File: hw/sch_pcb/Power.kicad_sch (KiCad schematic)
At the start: 55 parts, among them J3 HEADER_1x02, U10 TPS563249, U11 LTC3601, U12 NCP1117ST33, U9 LTC3601

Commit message: Renaming project to match name of new revision.
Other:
- title: QFHMIX01D -> QFHMIX01E
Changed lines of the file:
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@@
   (paper "A4")
   (title_block
-    (title "QFHMIX01D")
-    (date "2021-04-21")
+    (title "QFHMIX01E")
+    (date "2022-07-31")
     (comment 2 "Frontend for QFH active antenna")
   )

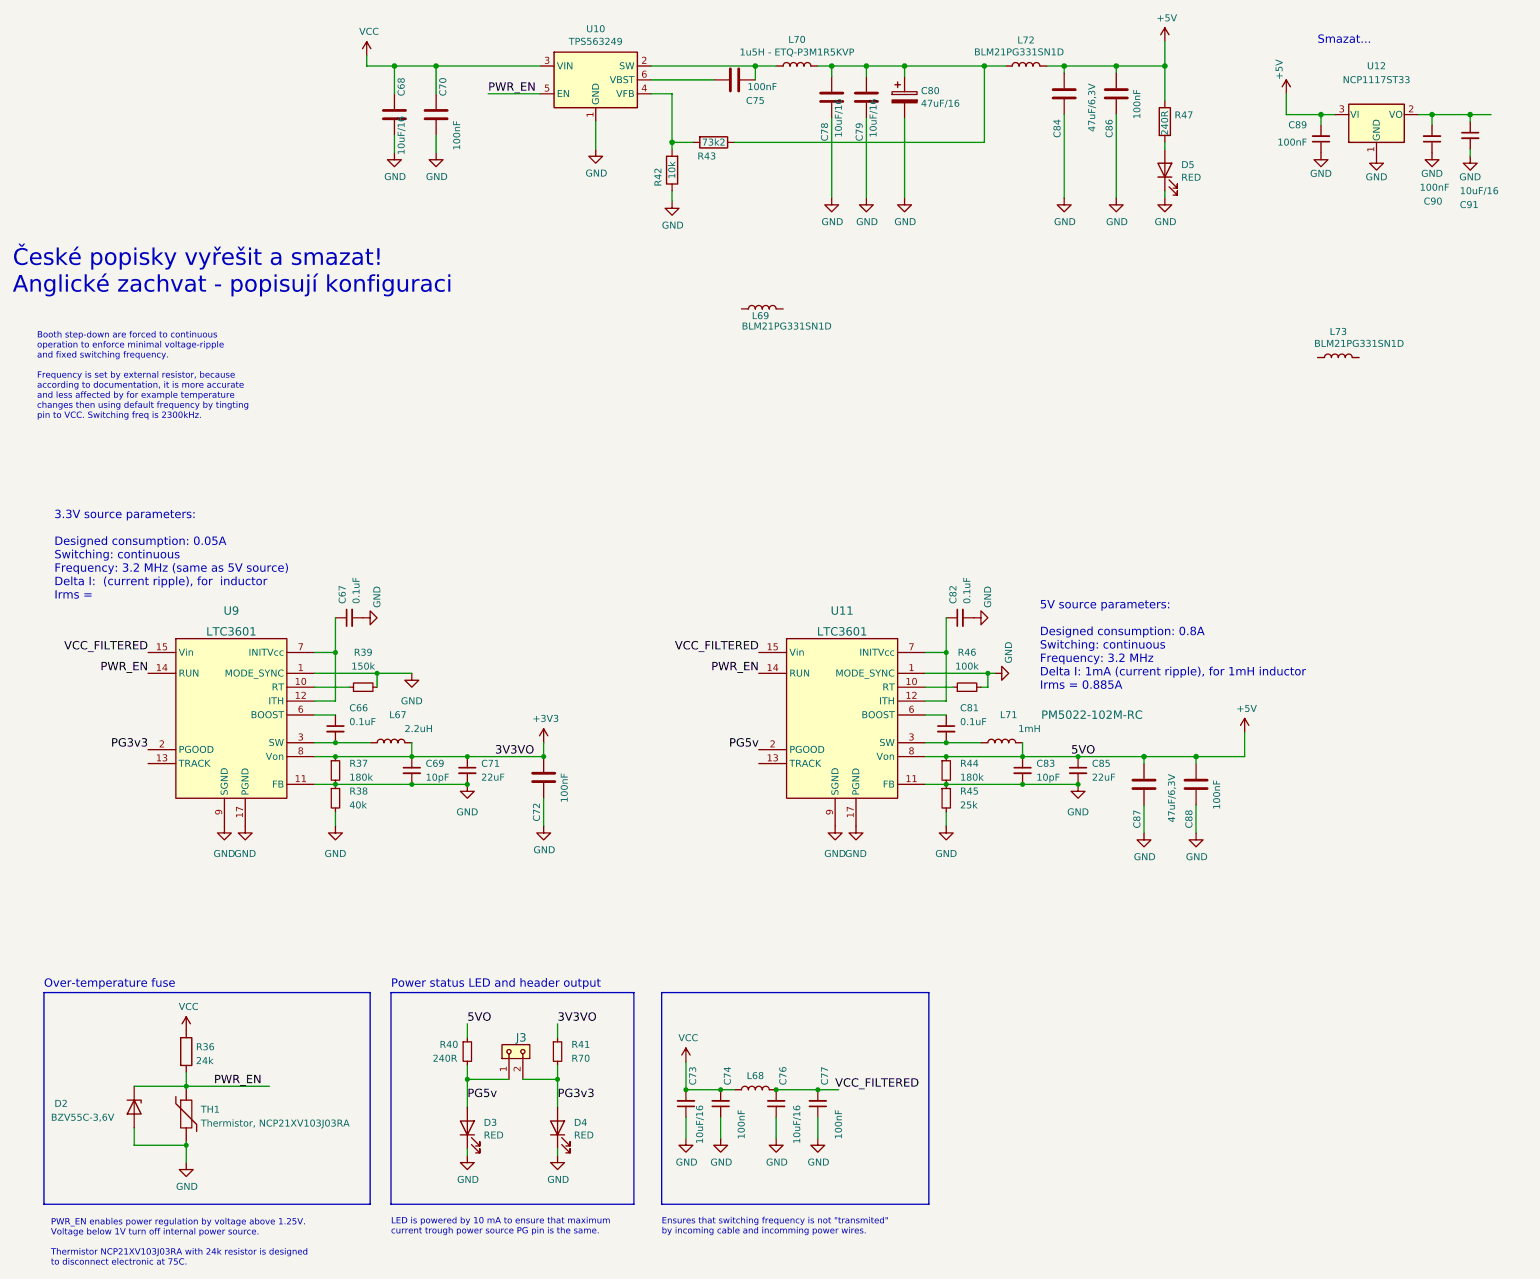
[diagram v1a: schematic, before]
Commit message: Add filter capacitors at swithinch power supply inputs.
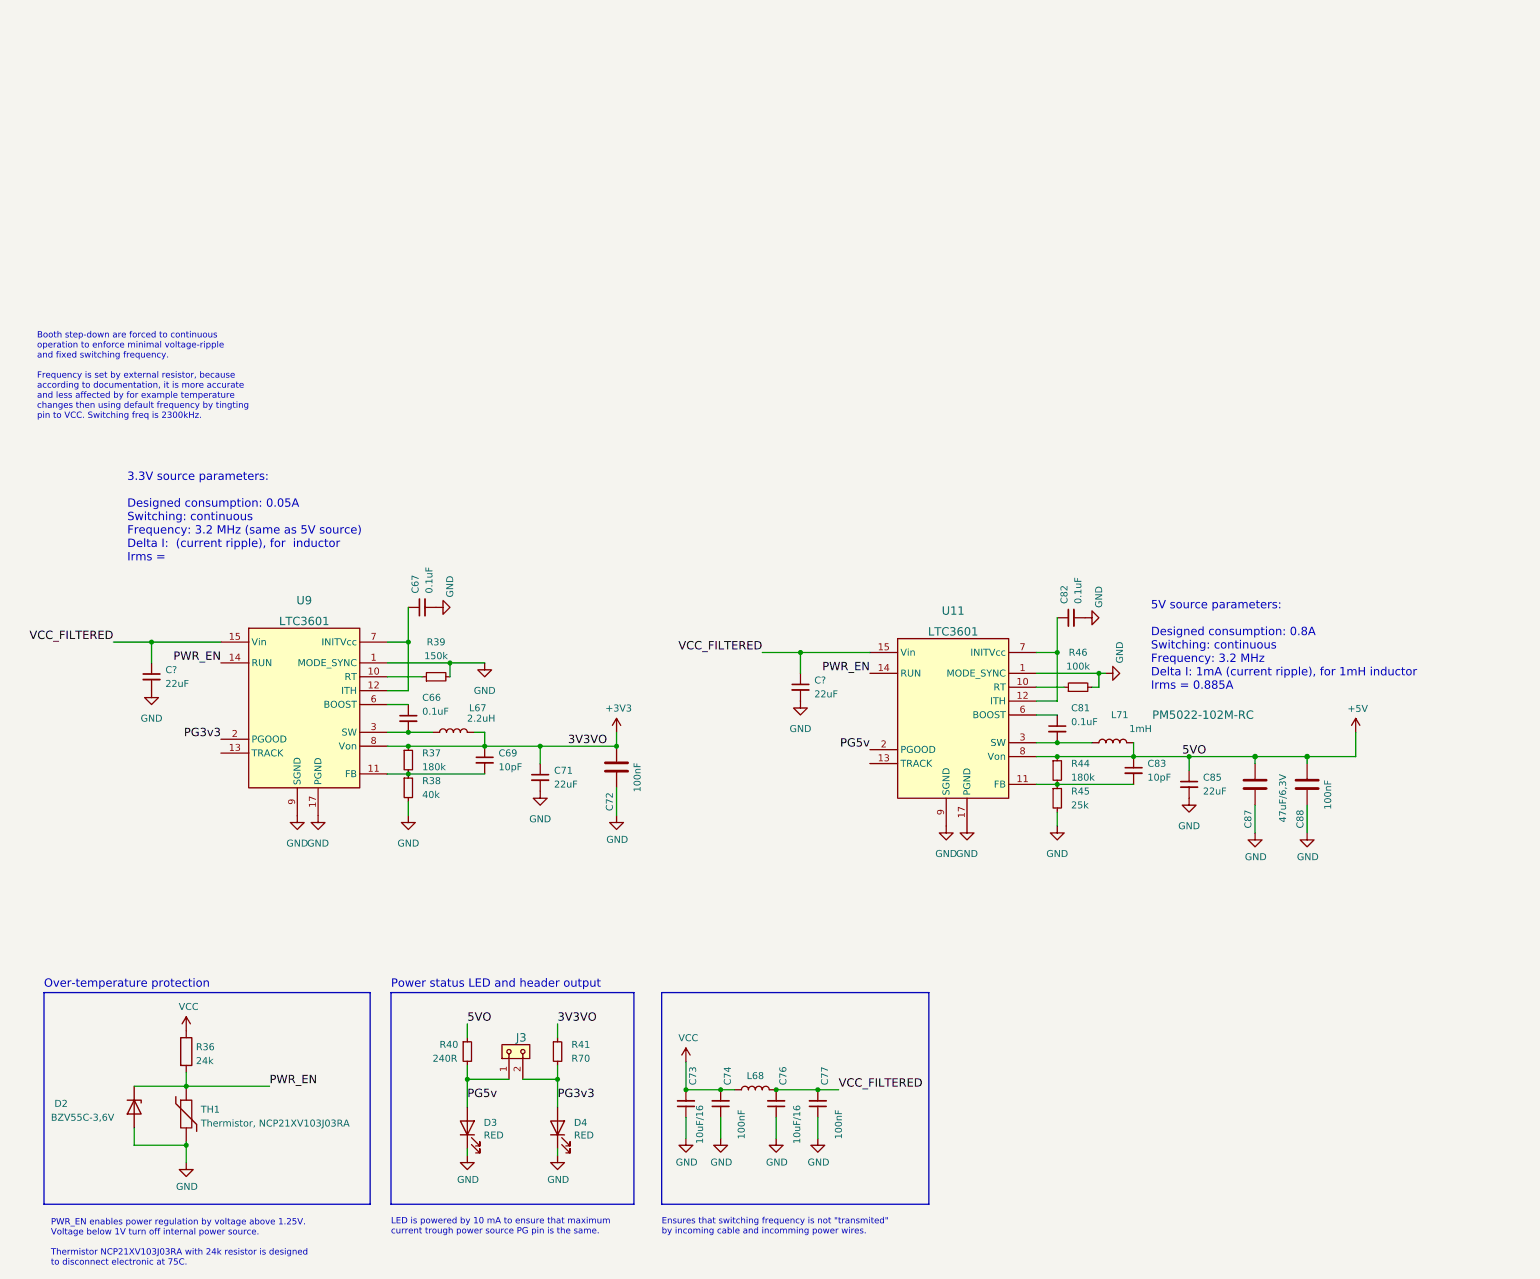
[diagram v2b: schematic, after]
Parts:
- removed C68, C78, C79: 10uF/16, Capacitor_SMD:C_0805_2012Metric, symbol Device:C
- removed C70, C75, C86: 100nF, Capacitor_SMD:C_0603_1608Metric, symbol Device:C
- removed C80: 47uF/16, Mlab_C:TantalC_SizeC_Reflow, symbol Device:CP
- removed C84: 47uF/6,3V, Capacitor_SMD:C_0805_2012Metric, symbol Device:C
- removed C89, C90: 100nF, Capacitor_SMD:C_0603_1608Metric, symbol QFHMIX01C-rescue:C_Small-device-QFHMIX01B-rescue
- removed C91: 10uF/16, Capacitor_SMD:C_0805_2012Metric, symbol QFHMIX01C-rescue:C_Small-device-QFHMIX01B-rescue
- removed D5: RED, Mlab_D:LED_1206, symbol Device:LED
- removed L69: BLM21PG331SN1D, Inductor_SMD:L_0805_2012Metric_Pad1.15x1.40mm_HandSolder, symbol QFHMIX01C-rescue:L-device-QFHMIX01B-rescue
- removed L70: 1u5H - ETQ-P3M1R5KVP, Mlab_L:PCC-M0530M-LP, symbol Device:L
- removed L72, L73: BLM21PG331SN1D, Inductor_SMD:L_0805_2012Metric_Pad1.15x1.40mm_HandSolder, symbol Device:L
- removed R42: 10k, Resistor_SMD:R_0603_1608Metric, symbol Device:R
- removed R43: 73k2, Resistor_SMD:R_0603_1608Metric, symbol Device:R
- removed R47: 240R, Resistor_SMD:R_0603_1608Metric, symbol Device:R
- removed U10: TPS563249, Package_TO_SOT_SMD:SOT-23-6, symbol Regulator_Switching:TPS563200
- removed U12: NCP1117ST33, Package_TO_SOT_SMD:SOT-223-3_TabPin2, symbol QFHMIX01C-rescue:AP1117-15-regul-QFHMIX01B-rescue
- added C? (x2): 22uF, symbol Device:C_Small
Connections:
- net GND: now also C?.2, C?.2; no longer C69.2, C83.2, R37.2, R38.1, R44.2, R45.1, U11.11 (FB), U9.11 (FB)
- net VCC_FILTERED: now also C?.1, C?.1
- new net: C83.2, R44.2, R45.1, U11.11 (FB)
- new net: C69.2, R37.2, R38.1, U9.11 (FB)
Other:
- note added: "Over-temperature protection"
- note removed: "Over-temperature fuse"
- note removed: "Smazat..."
- note removed: "České popisky vyřešit a smazat! Anglické zachvat - popisují konfiguraci"
- moved on the sheet: C66, C67, C69, C71, C72, C81, C82, C83, C85, C87, C88, L67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

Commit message: Change decrease impedance of feedback divider network.
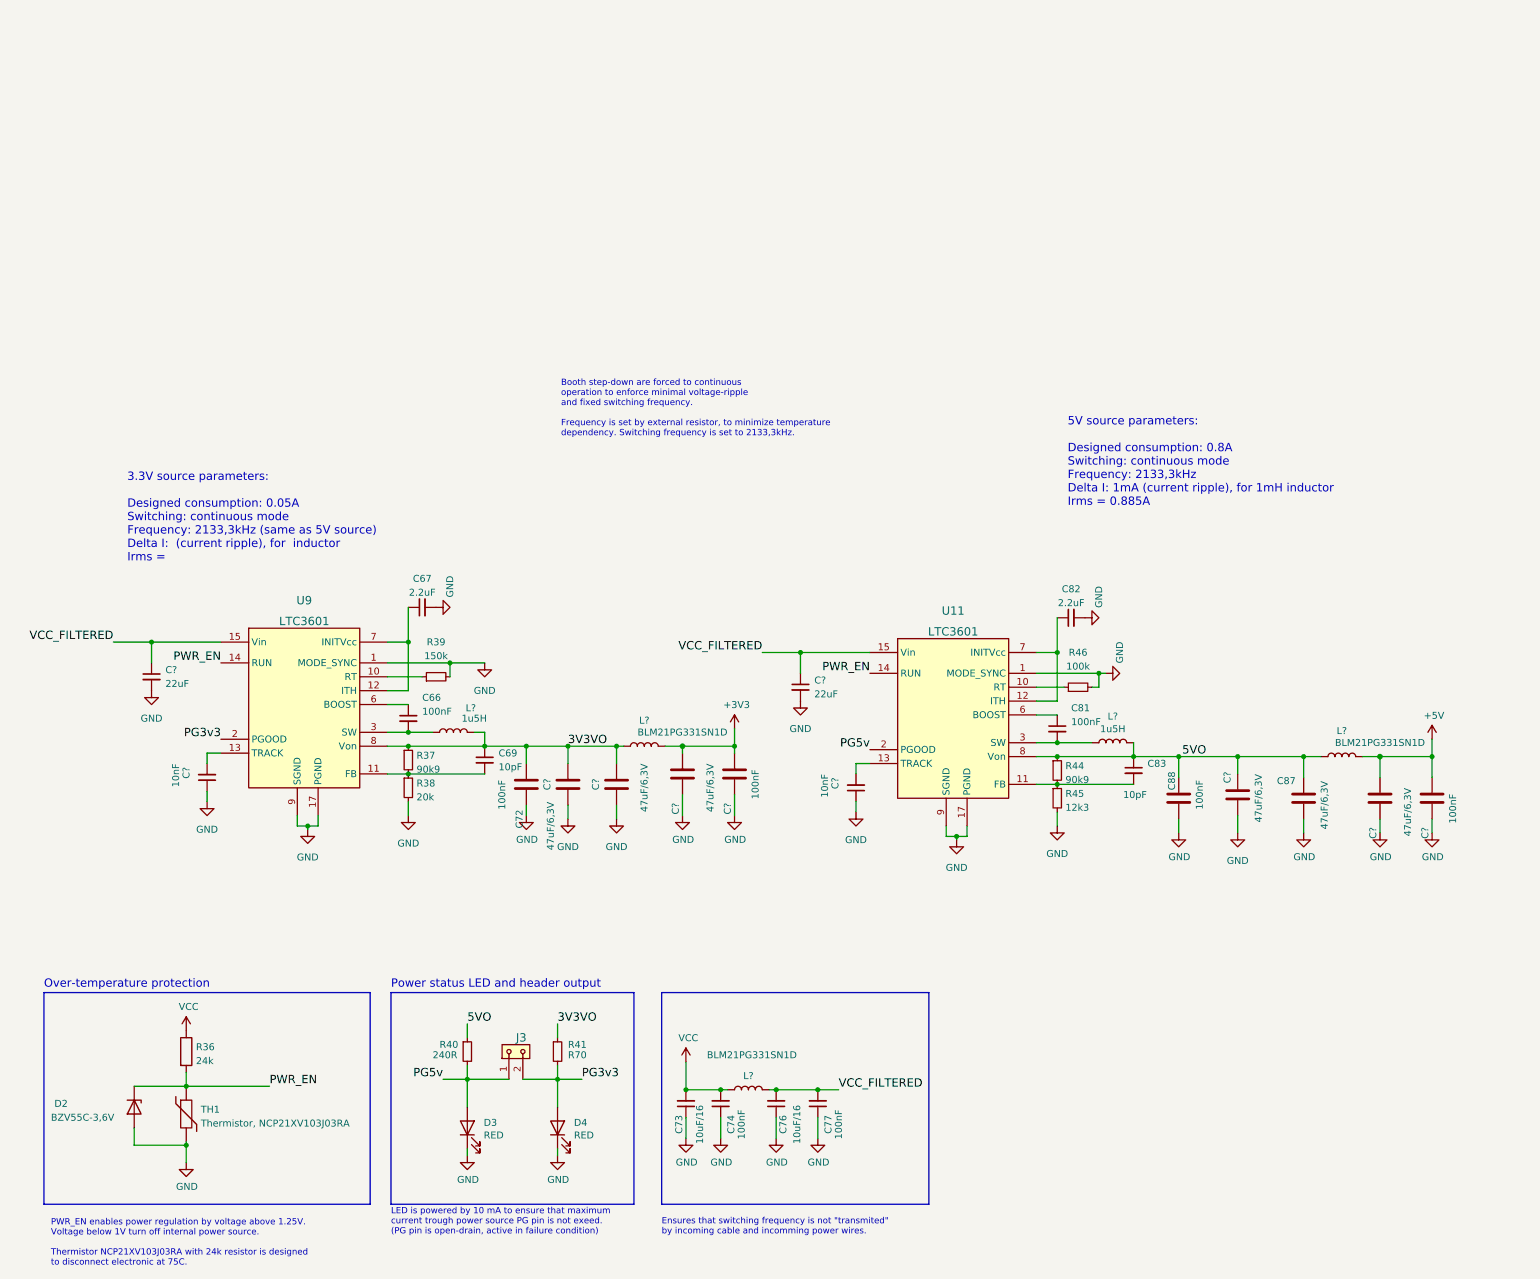
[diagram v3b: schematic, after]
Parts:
- removed C71, C85: 22uF, symbol Device:C_Small
- removed L67: 2.2uH, symbol Device:L
- removed L68: (no value), symbol Device:L
- removed L71: 1mH, symbol Device:L
- added C? (x2): 100nF, Capacitor_SMD:C_0603_1608Metric, symbol Device:C
- added C? (x5): 47uF/6,3V, Capacitor_SMD:C_0805_2012Metric, symbol Device:C
- added C? (x2): 10nF, Capacitor_SMD:C_0603_1608Metric, symbol QFHMIX01C-rescue:C_Small-device-QFHMIX01B-rescue
- added L? (x3): BLM21PG331SN1D, Inductor_SMD:L_0805_2012Metric_Pad1.15x1.40mm_HandSolder, symbol Device:L
- added L? (x2): 1u5H, Mlab_L:PCC-M0530M-LP, symbol Device:L
- C81: value 0.1uF -> 100nF
- C82: value 0.1uF -> 2.2uF
- R44: value 180k -> 90k9
- R45: value 25k -> 12k3
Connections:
- net +3V3: now also C?.2, C?.2, L?.2; no longer C69.1, C72.2, R37.1, R41.1, U9.8 (Von)
- net +5V: now also C?.2, C?.2, L?.2; no longer C83.1, C87.2, C88.2, R40.1, R44.1, U11.8 (Von)
- net GND: now also C?.1, C?.1, C?.1, C?.1, C?.1, C?.1, C?.1, C?.1, C?.1
- net VCC: now also L?.1
- net VCC_FILTERED: now also L?.2
- net at C66.2, U9.3 (SW), U9.4 (SW): now also L?.1
- net at U9.13 (TRACK): now also C?.2
- net at C81.2, U11.3 (SW), U11.4 (SW): now also L?.1
- net at U11.13 (TRACK): now also C?.2
- new net 3V3VO: C69.1, C72.2, C?.2, C?.2, L?.1, L?.2, R37.1, R41.1, U9.8 (Von)
- new net 5VO: C83.1, C87.2, C88.2, C?.2, L?.1, L?.2, R40.1, R44.1, U11.8 (Von)
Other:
- note added: "3.3V source parameters: Designed consumption: 0.05A Switching: continuous mode Frequency: 2133,3kHz (same as 5V source) Delta I: (current ripple), for inductor Irms ="
- note added: "5V source parameters: Designed consumption: 0.8A Switching: continuous mode Frequency: 2133,3kHz Delta I: 1mA (current ripple), for 1mH inductor Irms = 0.885A"
- note added: "Booth step-down are forced to continuous operation to enforce minimal voltage-ripple and fixed switching frequency. Frequency is set by external resistor, to minimize temperature dependency. Switching frequency is set to 2133,3kHz."
- note added: "LED is powered by 10 mA to ensure that maximum current trough power source PG pin is not exeed. (PG pin is open-drain, active in failure condition)"
- note removed: "3.3V source parameters: Designed consumption: 0.05A Switching: continuous Frequency: 3.2 MHz (same as 5V source) Delta I: (current ripple), for inductor Irms ="
- note removed: "5V source parameters: Designed consumption: 0.8A Switching: continuous Frequency: 3.2 MHz Delta I: 1mA (current ripple), for 1mH inductor Irms = 0.885A"
- note removed: "Booth step-down are forced to continuous operation to enforce minimal voltage-ripple and fixed switching frequency. Frequency is set by external resistor, because according to documentation, it is more accurate and less affected by for example temperature changes then using default frequency by tingting pin to VCC. Switching freq is 2300kHz."
- note removed: "LED is powered by 10 mA to ensure that maximum current trough power source PG pin is the same."
- moved on the sheet: C72, C87, C88
